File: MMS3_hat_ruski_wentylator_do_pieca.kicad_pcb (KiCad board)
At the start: 2 copper layers, 100 x 50 mm, 66 parts, among them J1 Chainbus in, J2 Chainbus Out, J3 Conn_01x04_Pin, J4 AMASS XT60 Male, J5 AMASS XT60 Female, J6 Conn_01x04_Socket, J7 Program, J9 Conn_01x06_Socket, Q1 AO3401A, Q2 FMMT493, U1 SN74CB3Q3245PWR, U2 M24C64, U3 XL6019E1, U4 AMS1117, U5 CH32V003F4U6, U6 MCP4161-502E/SN

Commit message: inital layout
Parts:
- removed L2: 47uH 5A, Inductor_SMD:L_10.4x10.4_H4.8
- removed R11, R2, R3, R5, R9: 10kΩ, PCM_JLCPCB:R_0402
- added L1: 47uH 5A, Inductor_SMD:L_12x12mm_H6mm, F.Cu at (116.0, 114.0)
- moved D1 131.4 mm to (81.5, 119.5), turned to -90 degrees
- moved TP5 116.9 mm to (120.0, 126.0)
- moved C4 115.2 mm to (120.5, 129.5), turned to 90 degrees
- moved TP4 115.0 mm to (123.0, 126.0)
- moved TP6 109.4 mm to (128.0, 130.0)
- moved U3 108.9 mm to (103.5, 114.0), turned to 90 degrees
- moved U6 107.9 mm to (123.5, 133.0)
- moved C11 105.9 mm to (105.2, 123.2), turned to -90 degrees
- moved C12 102.2 mm to (135.0, 115.5), turned to -90 degrees
- moved C9 96.3 mm to (91.0, 114.0), turned to 90 degrees
- moved C6 95.8 mm to (154.3, 127.6), turned to -90 degrees
- moved R24 95.4 mm to (151.8, 125.6), turned to 90 degrees
- moved D5 95.3 mm to (154.8, 117.6), turned to -90 degrees
- moved R23 94.8 mm to (152.8, 125.6), turned to -90 degrees
- moved R12 93.8 mm to (152.8, 121.6), turned to -90 degrees
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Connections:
- net Net-(D2-Pad2) renamed /Boost Converter/SW_NODE
- net Net-(U3-FB) renamed /Boost Converter/Feeback
- C11 pad 1: /Boost Converter/R_Var_GND -> /Boost Converter/Boost_In
- C9 pad 1: /Boost Converter/R_Var_GND -> /Boost Converter/Boost_In
- D1 pad 2: /Boost Converter/R_Var_GND -> /Boost Converter/Boost_In
- J4 pad 2: /Boost Converter/R_Var_GND -> /Boost Converter/Boost_In
- J5 pad 2: /Boost Converter/R_Var_GND -> /Boost Converter/Boost_In
- R18 pad 2: /Boost Converter/R_Var_GND -> GND
- R21 pad 1: /Boost Converter/R_Var_GND -> GND
- TP6 pad 1: /Boost Converter/R_Var_GND -> GND
- U3 pad 4: /Boost Converter/R_Var_GND -> /Boost Converter/Boost_In
- U6 pad 5: /Boost Converter/R_Var_GND -> GND
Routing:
- net BRD_VIN: track 0.00 -> 62.1 mm
- net /Boost Converter/Boost_In: track 0.00 -> 52.4 mm
- net /Boost Converter/Feeback: track 0.00 -> 24.8 mm, vias 0 -> 2
- net /Boost Converter/SW_NODE: track 0.00 -> 23.3 mm
- added copper zone on B.Cu, net /Boost Converter/Boost_In
- added copper zone on F.Cu, net /Boost Converter/Boost_In
- removed copper zone on B.Cu, net /Boost Converter/R_Var_GND
- removed copper zone on F.Cu, net /Boost Converter/R_Var_GND

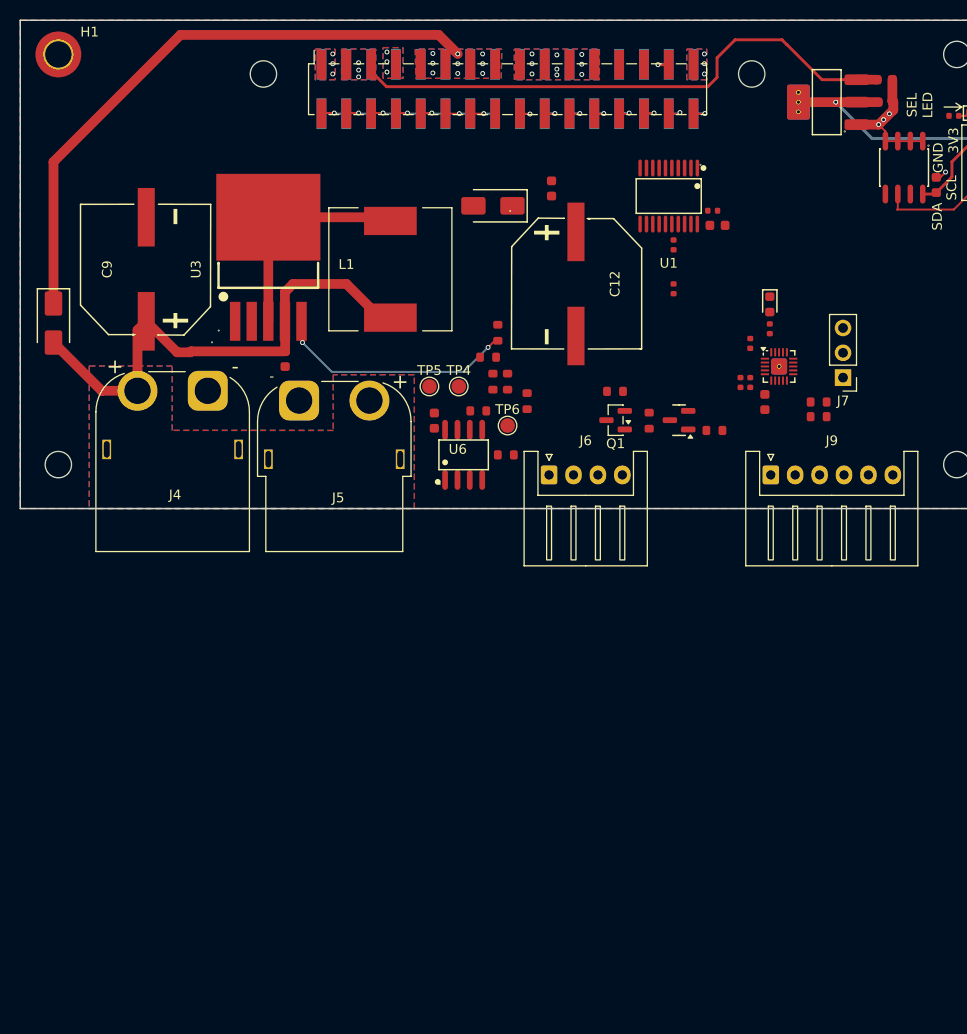
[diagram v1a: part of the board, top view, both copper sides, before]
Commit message: commit before removing all the diodes :"
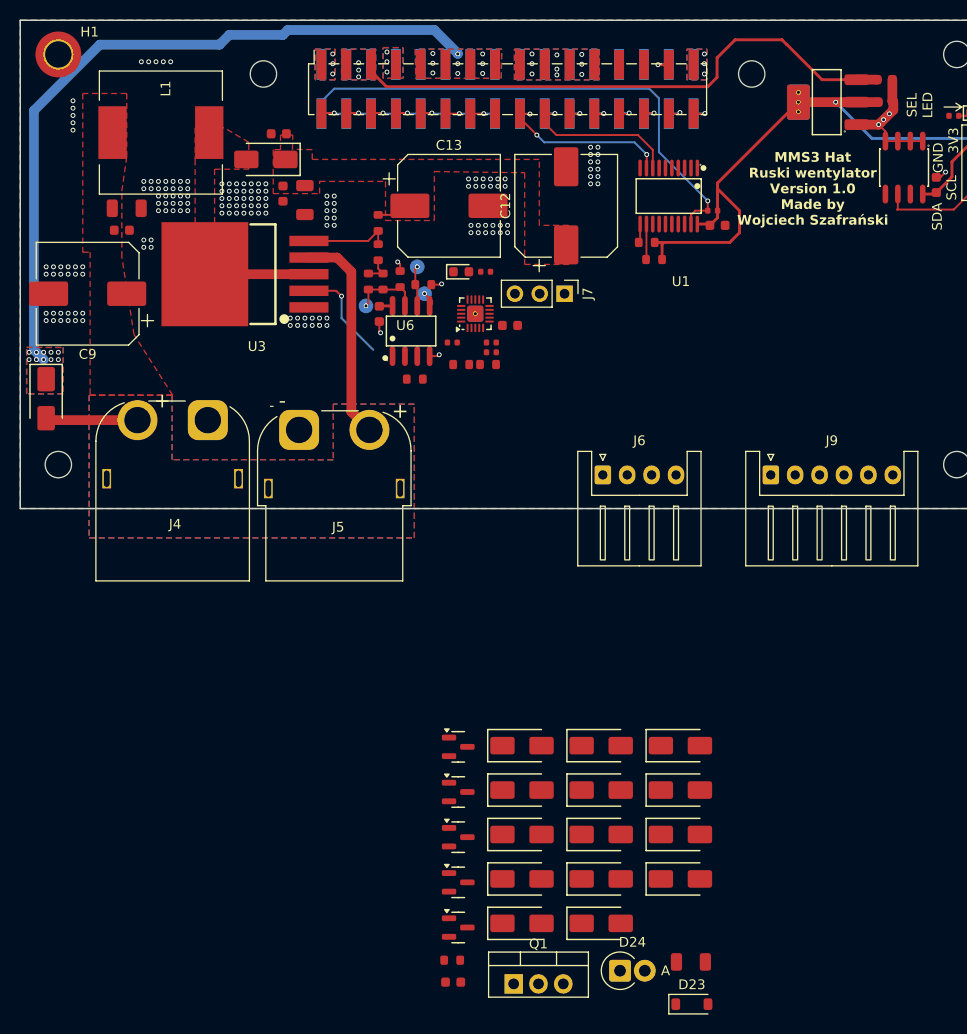
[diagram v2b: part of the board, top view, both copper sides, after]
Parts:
- removed Q2: FMMT493, PCM_JLCPCB:Q_SOT-23
- removed R10, R6: 10kΩ, PCM_JLCPCB:R_0402
- removed R22: 0Ω, PCM_JLCPCB:R_0603
- removed R25: 1kΩ, PCM_JLCPCB:R_0603
- removed R26: 10kΩ, PCM_JLCPCB:R_0603
- added C13: Whatever the chinese man has (preferably 220uF), Capacitor_SMD:CP_Elec_10x10, F.Cu at (122.0, 107.5)
- added C14: 10uF, PCM_JLCPCB:C_1206, F.Cu at (107.2, 106.9)
- added C15: 10uF, PCM_JLCPCB:C_1206, F.Cu at (89.0, 107.8)
- added C17: 1uF, PCM_JLCPCB:C_0603, F.Cu at (104.6, 100.1)
- added C20: 1uF, PCM_JLCPCB:C_0603, F.Cu at (122.4, 187.0)
- added C3: 10uF, PCM_JLCPCB:C_1206, F.Cu at (146.8, 184.9)
- added D12: US1M, PCM_JLCPCB:D_SMA, F.Cu at (129.5, 171.9)
- added D13: US1M, PCM_JLCPCB:D_SMA, F.Cu at (129.5, 176.4)
- added D14: US1M, PCM_JLCPCB:D_SMA, F.Cu at (129.5, 181.0)
- added D15: US1M, PCM_JLCPCB:D_SMA, F.Cu at (137.6, 162.8)
- added D16: US1M, PCM_JLCPCB:D_SMA, F.Cu at (137.6, 167.3)
- added D17: US1M, PCM_JLCPCB:D_SMA, F.Cu at (137.6, 171.9)
- added D18: US1M, PCM_JLCPCB:D_SMA, F.Cu at (137.6, 176.4)
- added D19: US1M, PCM_JLCPCB:D_SMA, F.Cu at (137.6, 181.0)
- added D20: US1M, PCM_JLCPCB:D_SMA, F.Cu at (145.7, 162.8)
- added D21: US1M, PCM_JLCPCB:D_SMA, F.Cu at (145.7, 167.3)
- added D23: D_Zener, Diode_SMD:D_SOD-123, F.Cu at (146.9, 189.2)
- added D24: D_Zener, Diode_THT:D_DO-15_P2.54mm_Vertical_AnodeUp, F.Cu at (139.5, 185.8)
- added D25: US1M, PCM_JLCPCB:D_SMA, F.Cu at (145.7, 171.9)
- added D26: US1M, PCM_JLCPCB:D_SMA, F.Cu at (145.7, 176.4)
- added D7: SS210, PCM_JLCPCB:D_SMA, F.Cu at (129.5, 162.8)
- added D8: SS210, PCM_JLCPCB:D_SMA, F.Cu at (129.5, 167.3)
- added Q10: AO3401A, PCM_JLCPCB:Q_SOT-23, F.Cu at (122.9, 167.5)
- added Q11: MMBT5401 200-300, PCM_JLCPCB:Q_SOT-23, F.Cu at (122.9, 172.2)
- added Q12: MMBT5551 200-300, PCM_JLCPCB:Q_SOT-23, F.Cu at (122.9, 176.8)
- added Q14: MMBT5551 200-300, PCM_JLCPCB:Q_SOT-23, F.Cu at (122.9, 181.4)
- added Q9: MMBT5551 200-300, PCM_JLCPCB:Q_SOT-23, F.Cu at (122.9, 162.9)
- added R2: 10kΩ, PCM_JLCPCB:R_0603, F.Cu at (143.0, 113.0)
- added R3: 10kΩ, PCM_JLCPCB:R_0603, F.Cu at (142.2, 111.2)
- added R5: 2.7kΩ, PCM_JLCPCB:R_0603, F.Cu at (122.3, 184.7)
- C12, C9: value EEVFK1J221Q -> Whatever the chinese man has (preferably 220uF); footprint EEVFK1J221Q:CAP-SMD_BD12.5-L13.5-W13.5-FD -> Capacitor_SMD:CP_Elec_10x10
- Q1: value AO3401A -> PMOS; footprint Package_TO_SOT_SMD:SOT-23 -> Package_TO_SOT_THT:TO-220-3_Vertical
- TP4, TP5, TP6: moved to B.Cu
- moved Q1 58.7 mm to (128.6, 187.2), turned to 0 degrees
- moved C10 44.2 mm to (88.5, 110.0), turned to 0 degrees
- moved R20 36.8 mm to (123.2, 123.8), turned to 180 degrees
- moved R4 34.3 mm to (126.0, 123.8)
- moved D5 31.8 mm to (123.2, 114.2), turned to 0 degrees
- moved U5 31.6 mm to (124.7, 118.5), turned to 90 degrees
- moved R12 30.5 mm to (122.3, 121.5), turned to 0 degrees
- moved J7 29.8 mm to (133.8, 116.5), turned to -90 degrees
- moved R13 29.7 mm to (125.8, 114.2), turned to 180 degrees
- moved L1 27.4 mm to (92.5, 100.0), turned to 0 degrees
- moved C6 27.3 mm to (128.2, 119.8), turned to 0 degrees
- moved R23 26.8 mm to (126.3, 121.5), turned to 0 degrees
- moved R24 25.7 mm to (126.3, 122.5), turned to 180 degrees
- moved D2 23.7 mm to (103.2, 102.8)
- moved R21 18.0 mm to (117.0, 115.0), turned to -90 degrees
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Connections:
- C10 pad 1: /Boost Converter/Boost_Out -> /Boost Converter/Boost_In
- C11 pad 1: /Boost Converter/Boost_In -> /Boost Converter/Boost_Out
- J1 pad 22: /Bus_switch/Chainbus_In.CS -> /Interboard_connector/Chainbus.CS
- J1 pad 24: /Bus_switch/Chainbus_In.SCK -> /Interboard_connector/Chainbus.SCK
- J1 pad 26: /Bus_switch/Chainbus_In.MOSI -> /Interboard_connector/Chainbus.MOSI
- J1 pad 28: /Bus_switch/Chainbus_In.MISO -> /Interboard_connector/Chainbus.MISO
- J1 pad 30: /Bus_switch/Chainbus_In.TX -> /Interboard_connector/Chainbus.TX
- J1 pad 32: /Bus_switch/Chainbus_In.RX -> /Interboard_connector/Chainbus.RX
- J2 pad 22: /Bus_switch/Chainbus_In.CS -> /Interboard_connector/Chainbus.CS
- J2 pad 24: /Bus_switch/Chainbus_In.SCK -> /Interboard_connector/Chainbus.SCK
- J2 pad 26: /Bus_switch/Chainbus_In.MOSI -> /Interboard_connector/Chainbus.MOSI
- J2 pad 28: /Bus_switch/Chainbus_In.MISO -> /Interboard_connector/Chainbus.MISO
- J2 pad 30: /Bus_switch/Chainbus_In.TX -> /Interboard_connector/Chainbus.TX
- J2 pad 32: /Bus_switch/Chainbus_In.RX -> /Interboard_connector/Chainbus.RX
- Q1 pad 1: Net-(Q1-G) -> /Boost Converter/Boost_Out
- Q1 pad 2: /Boost Converter/Boost_Out -> Net-(Q1-G)
- U1 pad 2: /Bus_switch/Chainbus_In.RX -> unconnected-(U1-A1-Pad2)
- U1 pad 3: /Bus_switch/Chainbus_In.TX -> unconnected-(U1-A2-Pad3)
- U1 pad 4: /Bus_switch/Chainbus_In.MISO -> unconnected-(U1-A3-Pad4)
- U1 pad 5: /Bus_switch/Chainbus_In.MOSI -> unconnected-(U1-A4-Pad5)
- U1 pad 6: /Bus_switch/Chainbus_In.SCK -> unconnected-(U1-A5-Pad6)
- U1 pad 7: /Bus_switch/Chainbus_In.CS -> unconnected-(U1-A6-Pad7)
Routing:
- net /Bus_switch/SEL1: track 0.00 -> 53.2 mm, vias 0 -> 1
- net +3V3: track 35.5 -> 71.9 mm
- net /Boost Converter/Boost_In: track 52.4 -> 31.3 mm
- net /Bus_switch/Chainbus_In.SDA: track 2.04 -> 18.4 mm, vias 1 -> 3
- net /Boost Converter/Feeback: track 24.8 -> 8.88 mm, vias 2 -> 0
- net /Bus_switch/Chainbus_In.SCL: track 2.09 -> 17.1 mm
- net /Boost Converter/SW_NODE: track 23.3 -> 10.7 mm
- net BRD_VIN: track 62.1 -> 73.8 mm, vias 9 -> 19
- net /Boost_En: track 0.00 -> 10.4 mm, vias 0 -> 1
- net /Boost Converter/R_Var_High: track 0.00 -> 7.27 mm, vias 0 -> 1
- net GND: track 14.5 -> 20.5 mm, vias 22 -> 187
- net Net-(U6-P0W): track 0.00 -> 4.17 mm, vias 0 -> 1
- net /Bus_switch/Chainbus.SCL: track 10.5 -> 14.2 mm
- net /Boost Converter/Boost_Out: track 0.00 -> 3.64 mm
- net Net-(R16-Pad2): track 0.00 -> 3.07 mm
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- added copper zone on F.Cu, net /Boost Converter/Boost_Out
- added copper zone on F.Cu, net /Boost Converter/SW_NODE
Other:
- board text added: "MMS3 Hat Ruski wentylator Version 1.0 Made by Wojciech Szafrański"

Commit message: finished routing
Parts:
- removed C20: 1uF, PCM_JLCPCB:C_0603
- removed D12, D13, D14, D15, D16, D17, D18, D19, D20, D21, D25, D26: US1M, PCM_JLCPCB:D_SMA
- removed D23: D_Zener, Diode_SMD:D_SOD-123
- removed D24: D_Zener, Diode_THT:D_DO-15_P2.54mm_Vertical_AnodeUp
- removed D7, D8: SS210, PCM_JLCPCB:D_SMA
- removed Q14: MMBT5551 200-300, PCM_JLCPCB:Q_SOT-23
- added C5: 12pF, PCM_JLCPCB:C_0603, F.Cu at (167.3, 119.9)
- added R6: 0Ω, PCM_JLCPCB:R_0603, F.Cu at (145.6, 125.7)
- added R7: 1kΩ, PCM_JLCPCB:R_0603, F.Cu at (133.0, 128.7)
- added R8: 3.3kΩ, PCM_JLCPCB:R_0603, F.Cu at (141.6, 122.8)
- added S1: Tactile Button, 160gf, PCM_JLCPCB:SW_TS-1088-AR02016, F.Cu at (172.1, 117.4)
- added X2: X322525MOB4SI, PCM_JLCPCB:OSC-SMD_4P-L3.2-W2.5-BL, F.Cu at (167.4, 117.5)
- C3: value 10uF -> 12pF; footprint PCM_JLCPCB:C_1206 -> PCM_JLCPCB:C_0603
- R5: value 2.7kΩ -> 1kΩ
- U5: value CH32V003F4U6 -> CH32V003FxPx; footprint PCM_JLCPCB:QFN-20-1EP_3x3mm_P0.4mm_EP1.65x1.65mm -> PCM_JLCPCB:TSSOP-20_4.4x6.5mm_P0.65mm
- moved C3 72.8 mm to (167.4, 115.1), turned to 180 degrees
- moved G*** 70.1 mm to (97.1, 114.1)
- moved R5 62.9 mm to (132.4, 122.7), turned to -90 degrees
- moved Q1 62.8 mm to (150.5, 128.3), turned to 90 degrees
- moved Q12 51.7 mm to (133.2, 126.2)
- moved D5 49.6 mm to (172.3, 121.3), turned to 180 degrees
- moved R12 47.6 mm to (169.9, 119.1), turned to -90 degrees
- moved Q11 47.1 mm to (137.4, 127.3)
- moved Q10 46.1 mm to (142.3, 125.7), turned to 180 degrees
- moved R13 44.6 mm to (169.7, 121.6), turned to 0 degrees
- moved Q9 41.9 mm to (137.6, 123.7), turned to 180 degrees
- moved C6 37.0 mm to (164.9, 114.5), turned to 90 degrees
- moved R17 37.0 mm to (154.8, 118.0), turned to -90 degrees
- moved U5 35.6 mm to (160.3, 117.8), turned to 180 degrees
- moved R20 31.6 mm to (154.7, 126.3), turned to 90 degrees
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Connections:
- C3 pad 1: /High side switch/V_low_mosfet -> /CH32V003/OSCO
- Q1 pad 1: /Boost Converter/Boost_Out -> /CN_MOT_VCC
- Q1 pad 3: /CN_MOT_VCC -> /Boost Converter/Boost_Out
- Q11 pad 2: /Boost Converter/Boost_Out -> Net-(Q1-G)
- Q11 pad 3: Net-(Q1-G) -> GND
- Q12 pad 2: GND -> Net-(Q12-E)
- Q12 pad 3: Net-(Q12-C) -> Net-(Q11-B)
- Q9 pad 1: Net-(Q9-B) -> Net-(Q11-B)
- Q9 pad 2: /High side switch/V_low_mosfet -> Net-(Q1-G)
- Q9 pad 3: Net-(Q1-G) -> /Boost Converter/Boost_Out
- R5 pad 1: Net-(Q14-E) -> /PWM_Mosfet_gate
- R5 pad 2: GND -> Net-(Q12-B)
- U5 pad 1: /CH32V003/PD7 -> /PD4
- U5 pad 10: /Boost_En -> /PWM_Mosfet_gate
- U5 pad 11: /CH32V003/PC4 -> /Bus_switch/Chainbus.SCL
- U5 pad 12: /Boost Converter/CH32V003.SCK -> /Bus_switch/Chainbus.SDA
- U5 pad 13: /Boost Converter/CH32V003.MOSI -> /Boost_En
- U5 pad 14: /Boost Converter/CH32V003.MISO -> /CH32V003/PC4
- U5 pad 15: /CH32V003/SWIO -> /Boost Converter/CH32V003.SCK
- U5 pad 16: /SPI_NOT_CS -> /Boost Converter/CH32V003.MOSI
- U5 pad 17: /PD3 -> /Boost Converter/CH32V003.MISO
- U5 pad 18: /PD4 -> /CH32V003/SWIO
- U5 pad 19: /PD5 (TX) -> /SPI_NOT_CS
- U5 pad 2: /CH32V003/OSCI -> /PD5 (TX)
- U5 pad 20: /PD6 (RX) -> /PD3
- U5 pad 3: /CH32V003/OSCO -> /PD6 (RX)
- U5 pad 4: GND -> /CH32V003/PD7
- U5 pad 5: /Hall_out -> /CH32V003/OSCI
- U5 pad 6: +3V3 -> /CH32V003/OSCO
- U5 pad 7: /PWM_Mosfet_gate -> GND
- U5 pad 8: /Bus_switch/Chainbus.SCL -> /Hall_out
- U5 pad 9: /Bus_switch/Chainbus.SDA -> +3V3
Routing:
- net +3V3: track 71.9 -> 194.4 mm, vias 1 -> 4
- net +5V: track 57.3 -> 148.6 mm, vias 3 -> 5
- net /Bus_switch/Chainbus.SDA: track 1.94 -> 54.4 mm, vias 0 -> 2
- net /SPI_NOT_CS: track 0.00 -> 48.7 mm, vias 0 -> 2
- net /Boost Converter/CH32V003.MISO: track 0.00 -> 45.6 mm, vias 0 -> 2
- net /Boost_En: track 10.4 -> 56.0 mm, vias 1 -> 2
- net /Boost Converter/CH32V003.SCK: track 0.00 -> 45.4 mm, vias 0 -> 2
- net /Bus_switch/Chainbus.SCL: track 14.2 -> 55.9 mm
- net /Boost Converter/Boost_Out: track 3.64 -> 43.6 mm
- net /PWM_Mosfet_gate: track 0.00 -> 35.1 mm, vias 0 -> 4
- net /Bus_switch/SEL1: track 53.2 -> 82.6 mm, vias 1 -> 2
- net /CN_MOT_VCC: track 0.00 -> 24.8 mm
- net Net-(Q1-G): track 0.00 -> 21.9 mm, vias 0 -> 3
- net /PD6 (RX): track 0.00 -> 20.8 mm
- net /Hall_out: track 0.00 -> 19.5 mm
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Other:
- board text added: "GND | 5V | Vmot | Hal"
- board text added: "PD6|PD5|PD4|PD3|3V3|GND"

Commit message: minor fixes etc
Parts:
- removed R8: 3.3kΩ, PCM_JLCPCB:R_0603
- moved R7 10.4 mm to (141.6, 122.8), turned to 0 degrees
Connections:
- Q12 pad 2: Net-(Q12-E) -> GND
- R7 pad 1: GND -> Net-(Q11-B)
- R7 pad 2: Net-(Q12-E) -> /Boost Converter/Boost_Out
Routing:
- net Net-(Q12-E): track 1.61 -> 0.00 mm
- net GND: track 36.0 -> 35.0 mm, vias 272 -> 271
